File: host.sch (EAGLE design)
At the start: 25 parts, among them IC10 74LVC1T45W6-7, IC11 74LVC1T45W6-7, IC12 74LVC1T45W6-7, IC2 NCP187AMT120TAG, IC3 LD39200PU33R, IC8 74LVC1T45W6-7, Y1 DSC6001J

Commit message: Add the level changes (mostly, still need decoupling and connection to FPGA)
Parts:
- removed IC12: 74LVC1T45W6-7, samacsys:74LVC1T45W6-7
- added C13, C14, C15, C16, C17, C18: 100nF, rcl:C-EUC0201
- added IC1, IC4, IC5, IC6, IC9: 74LVC1T45GS,132, host:74LVC1T45GS,132
- added IC7: 74ALVC164245DGG:11, samacsys:74ALVC164245DGG_11
- IC10, IC11: value 74LVC1T45W6-7 -> 74LVC1T45GS,132; device samacsys:74LVC1T45W6-7 -> host:74LVC1T45GS,132; USE 74LVC1T45W6-7 -> (none)
- IC8: value 74LVC1T45W6-7 -> 74ALVC164245DGG:11; device samacsys:74LVC1T45W6-7 -> samacsys:74ALVC164245DGG_11; USE 74LVC1T45W6-7 -> 74ALVC164245DGG:11
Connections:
- new net !EXTSEL!: IC10.A
- new net !IRQ!: IC11.A
- new net !MPD!: IC9.A
- new net DIR_EXTSEL: IC10.DIR
- new net DIR_IRQ: IC11.DIR
- new net DIR_MPD: IC9.DIR
- net !A8_CCTL!: now also IC7.1B1
- net !A8_CLK!: now also IC7.1B2
- net !A8_D1XX!: now also IC7.1B0
- net !A8_EXTSEL!: now also IC10.B
- net !A8_HALT!: now also IC1.B; no longer IC8.B
- net !A8_IRQ!: now also IC11.B
- net !A8_MPD!: now also IC9.B
- net !A8_REF!: now also IC6.B; no longer IC10.B
- net !A8_RESET!: now also IC5.B; no longer IC11.B
- net !A8_S4!: now also IC7.1B5
- net !A8_S5!: now also IC7.1B4
- net !HALT!: now also IC1.A; no longer IC8.A
- net !REF!: now also IC6.A; no longer IC10.A
- net !RESET!: now also IC5.A; no longer IC11.A
- net +3V3: now also C14.1, C16.1, C18.1, IC1.VCC(A), IC4.VCC(A), IC5.VCC(A), IC6.VCC(A), IC9.VCC(A); no longer IC12.VCC(A), IC8.VCC(A)
- net +5V: now also C13.1, C15.1, C17.1, IC1.VCC(B), IC4.VCC(B), IC5.VCC(B), IC6.VCC(B), IC9.VCC(B); no longer IC12.VCC(B), IC8.VCC(B)
- net A8_A0: now also IC8.2B2
- net A8_A1: now also IC8.2B4
- net A8_A10: now also IC8.1B3
- net A8_A11: now also IC8.1B4
- net A8_A12: now also IC8.1B5
- net A8_A13: now also IC8.1B2
- net A8_A14: now also IC8.1B1
- net A8_A15: now also IC8.1B0
- net A8_A2: now also IC8.2B6
- net A8_A3: now also IC8.2B7
- net A8_A4: now also IC8.2B5
- net A8_A5: now also IC8.2B3
- net A8_A6: now also IC8.2B1
- net A8_A7: now also IC8.2B0
- net A8_A8: now also IC8.1B7
- net A8_A9: now also IC8.1B6
- net A8_D0: now also IC7.2B3
- net A8_D1: now also IC7.2B4
- net A8_D2: now also IC7.2B5
- net A8_D3: now also IC7.2B2
- net A8_D4: now also IC7.2B7
- net A8_D5: now also IC7.2B6
- net A8_D6: now also IC7.2B1
- net A8_D7: now also IC7.2B0
- net A8_R/!W!: now also IC4.B; no longer IC12.B
- net A8_RD4: now also IC7.1B6
- net A8_RD5: now also IC7.1B3
- net DIR_HALT: now also IC1.DIR; no longer IC8.DIR
- net DIR_REF: now also IC6.DIR; no longer IC10.DIR
- net DIR_RST: now also IC5.DIR; no longer IC11.DIR
- net DIR_RW: now also IC4.DIR; no longer IC12.DIR
- net GND: now also IC4.GND, IC5.GND, IC6.GND; no longer IC10.GND, IC11.GND, IC12.GND, IC8.GND
- net GND1: now also C13.2, C14.2, C15.2, C16.2, C17.2, C18.2, IC1.GND, IC10.GND, IC11.GND, IC9.GND
- net R/!W!: now also IC4.A; no longer IC12.A
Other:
- moved on the sheet: C10, C11, C12, C7, C8, C9, IC10, IC11

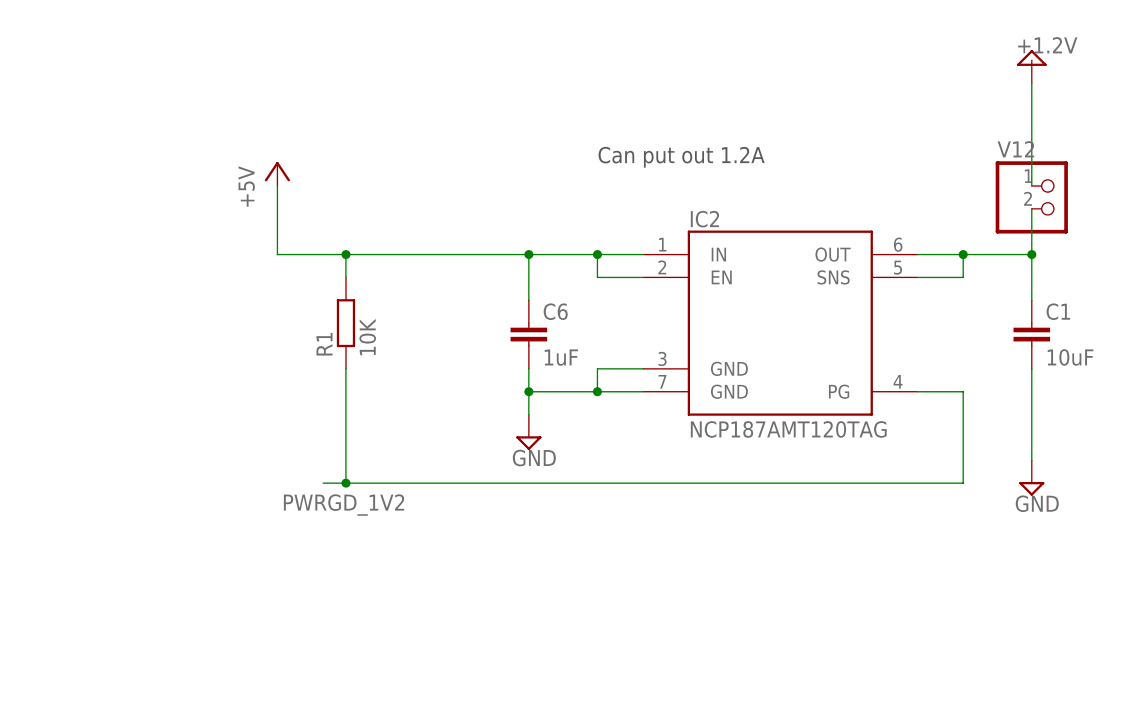
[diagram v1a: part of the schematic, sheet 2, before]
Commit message: Move to 6-layer board for supply cleanliness
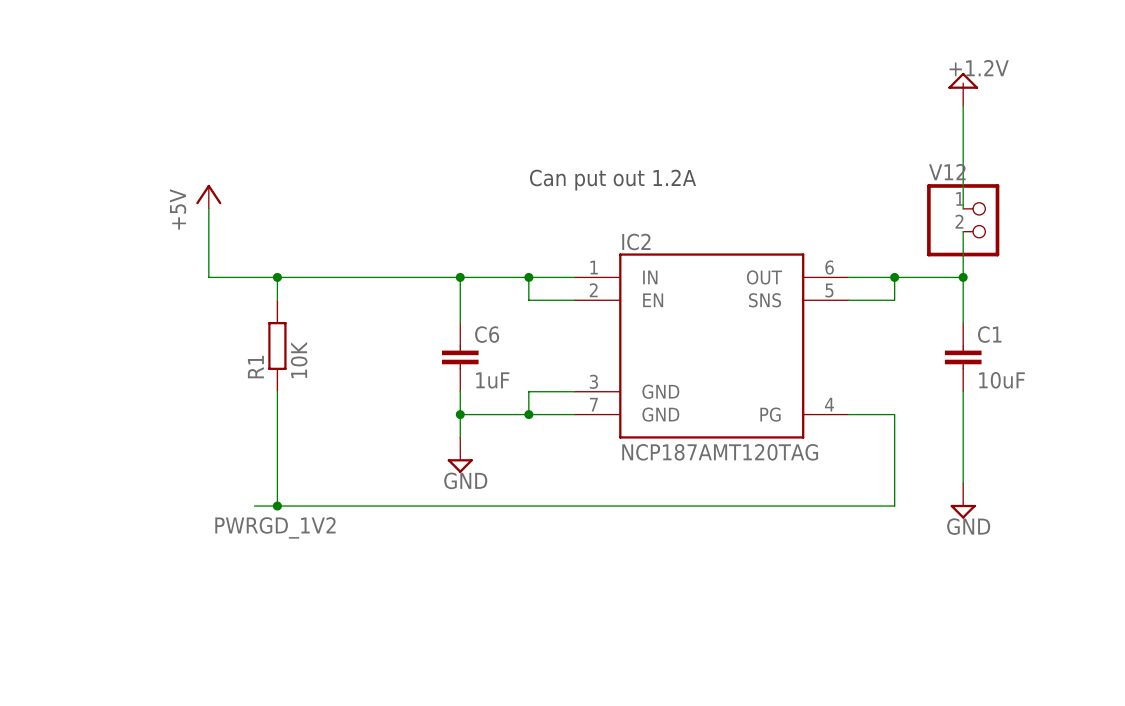
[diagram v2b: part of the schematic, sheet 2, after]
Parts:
- IC2: ARROW_PART_NUMBER (none) -> NCP187AMT120TAG
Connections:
- removed net GND1: C11.2, C12.2, C13.2, C14.2, C15.2, C16.2, C17.2, C18.2, IC1.GND, IC10.GND, IC11.GND, IC9.GND
- net +1.2V: now also U$1-CFG.VCC@125, U$1-CFG.VCC@128, U$1-CFG.VCC@13, U$1-CFG.VCC@130, U$1-CFG.VCC@22, U$1-CFG.VCC@49, U$1-CFG.VCC@57, U$1-CFG.VCC@85, U$1-CFG.VCC@96, U$1-CFG.VCCA_BR@73, U$1-LEFT.VCCA_TL@2, U$1-TOP.VCCA_TR@107
- net +5V: now also IC7.VCC(B)@18, IC7.VCC(B)@7, IC8.VCC(B)@18, IC8.VCC(B)@7
- net CLK25: now also U$1-TOP.GPIOR_157_PLLIN@75; no longer U$1-RIGHT.GPIOL_74_PLLIN0@132
- net GND: now also C11.2, C12.2, C13.2, C14.2, C15.2, C16.2, C17.2, C18.2, IC1.GND, IC10.GND, IC11.GND, IC9.GND
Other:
- moved on the sheet: C1, C6, IC2, R1, V12

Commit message: Hook up the level-translators to the FPGA
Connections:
- new net !CCTL!: IC7.1A1, U$1-RIGHT.GPIOR_85@111
- new net !D1XX!: IC7.1A0, U$1-RIGHT.GPIOR_86@112
- new net !S4!: IC7.1A5, U$1-RIGHT.GPIOR_79_EXTFB1_CDI30@118
- new net !S5!: IC7.1A4, U$1-RIGHT.GPIOR_80@117
- new net A0: IC8.2A2, U$1-LEFT.GPIOL_31_CLK7_CDI6@11
- new net A1: IC8.2A4, U$1-LEFT.GPIOL_24_CLK0@15
- new net A10: IC8.1A3, U$1-RIGHT.GPIOL_64@144
- new net A11: IC8.1A4, U$1-LEFT.GPIOL_53_CDI10@3
- new net A12: IC8.1A5, U$1-LEFT.GPIOL_54_CDI11@4
- new net A13: IC8.1A2, U$1-RIGHT.GPIOL_66_CDI12@142
- new net A14: IC8.1A1, U$1-RIGHT.GPIOL_65@141
- new net A15: IC8.1A0, U$1-RIGHT.GPIOL_67_CDI13@140
- new net A2: IC8.2A6, U$1-LEFT.GPIOL_21_CTRL1_CDI5@17
- new net A3: IC8.2A7, U$1-LEFT.GPIOL_20_CTRL0_CDI4@18
- new net A4: IC8.2A5, U$1-LEFT.GPIOL_22_CTRL2@16
- new net A5: IC8.2A3, U$1-LEFT.GPIOL_25_CLK1@14
- new net A6: IC8.2A1, U$1-LEFT.GPIOL_32_CTRL4_CDI7@10
- new net A7: IC8.2A0, U$1-LEFT.GPIOL_40_CDI8@8
- new net A8: IC8.1A7, U$1-LEFT.GPIOL_41_CDI9@7
- new net A9: IC8.1A6, U$1-LEFT.GPIOL_46@6
- new net CLK: IC7.1A2, U$1-RIGHT.GPIOR_84@113
- new net D0: IC7.2A3, U$1-RIGHT.GPIOL_74_PLLIN0@132
- new net D1: IC7.2A4, U$1-RIGHT.GPIOL_73_EXTFB1_CDI15@134
- new net D2: IC7.2A5, U$1-RIGHT.GPIOL_72_EXTFB0_CDI14@135
- new net D3: IC7.2A2, U$1-RIGHT.GPIOL_75_PLLIN1@131
- new net D4: IC7.2A7, U$1-RIGHT.GPIOL_70_CBSEL0@137
- new net D5: IC7.2A6, U$1-RIGHT.GPIOL_71_!STATUS!@136
- new net D6: IC7.2A1, U$1-RIGHT.GPIOR_76_PLLIN0@124
- new net D7: IC7.2A0, U$1-RIGHT.GPIOR_77_PLLIN1@123
- new net DIR_A: IC8.1DIR, IC8.2DIR, U$1-RIGHT.GPIOL_68@139
- new net DIR_D: IC7.2DIR, U$1-RIGHT.GPIOL_69_CBSEL1@138
- new net DIR_IN: IC7.1DIR, U$1-RIGHT.GPIOR_87_CDI29@110
- new net RD4: IC7.1A6, U$1-RIGHT.GPIOR_78_EXTFB0_CDI31@119
- new net RD5: IC7.1A3, U$1-RIGHT.GPIOR_83@114
- net !EXTSEL!: now also U$1-TOP.GPIOR_94_CDI27@106
- net !HALT!: now also U$1-TOP.GPIOR_116_CTRL15@99
- net !IRQ!: now also U$1-TOP.GPIOR_104_CDI25@103
- net !MPD!: now also U$1-TOP.GPIOR_122_CLK13_CDI21@97
- net !REF!: now also U$1-TOP.GPIOR_125_CLK10@92
- net !RESET!: now also U$1-TOP.GPIOR_112_CDI23@101
- net +3V3: now also U$1-LEFT.VCCIO1B@21, U$1-LEFT.VCCIO1C_1D@12, U$1-RIGHT.VCCIO1E@143, U$1-RIGHT.VCCIO3A@122, U$1-TOP.VCCIO3B_3C@95, U$1-TOP.VCCIO3D@91, U$1-TOP.VCCIO3E@88
- net DIR_EXTSEL: now also U$1-RIGHT.GPIOR_88_CDI28@109
- net DIR_HALT: now also U$1-TOP.GPIOR_113_CDI22@100
- net DIR_IRQ: now also U$1-TOP.GPIOR_95_CDI26@105
- net DIR_MPD: now also U$1-TOP.GPIOR_117_CTRL14@98
- net DIR_REF: now also U$1-TOP.GPIOR_123_CLK12_CDI20@93
- net DIR_RST: now also U$1-TOP.GPIOR_105_CDI24@102
- net DIR_RW: now also U$1-RIGHT.GPIOR_81_MREFCLK@116
- net GND: now also IC7.GND@10, IC7.GND@15, IC7.GND@21, IC7.GND@28, IC7.GND@34, IC7.GND@39, IC7.GND@4, IC7.GND@45, IC8.GND@10, IC8.GND@15, IC8.GND@21, IC8.GND@28, IC8.GND@34, IC8.GND@39, IC8.GND@4, IC8.GND@45
- net R/!W!: now also U$1-RIGHT.GPIOR_82@115
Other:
- note added: "OE on 8-bit LT's decoupling on 8-bit LTs SPI hookup in 4-bit mode pull resistors decoupling on FPGA USB-C connector TTAG / JTAG / SPI CDONE, CRESET, Leds"
- note removed: "input: CLK !CCTL! RD4 RD5 output: !MPD! !EXTSEL! !IRQ! inout: !RESET! R/!W! !HALT! !REF! A[0..15] D[0..7]"

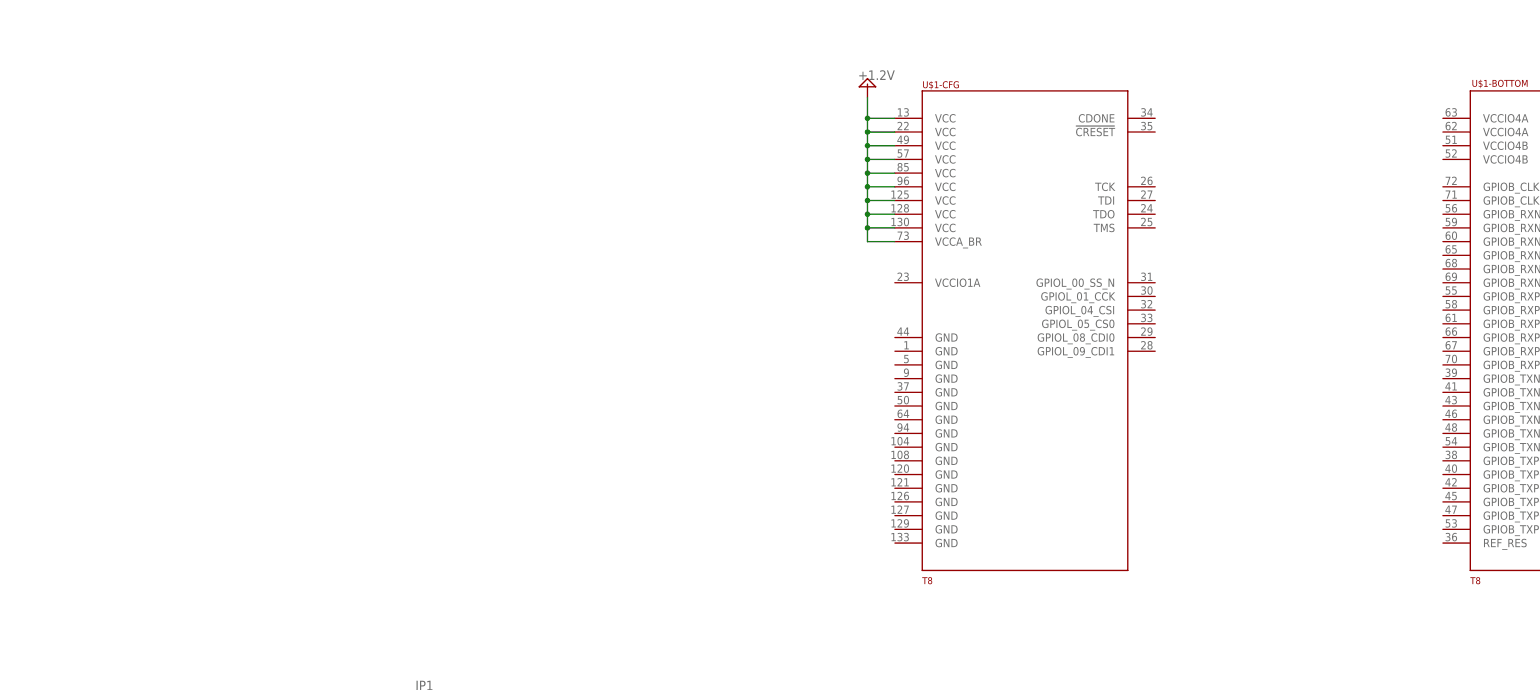
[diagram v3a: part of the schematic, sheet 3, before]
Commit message: Add FPGA decoupling caps
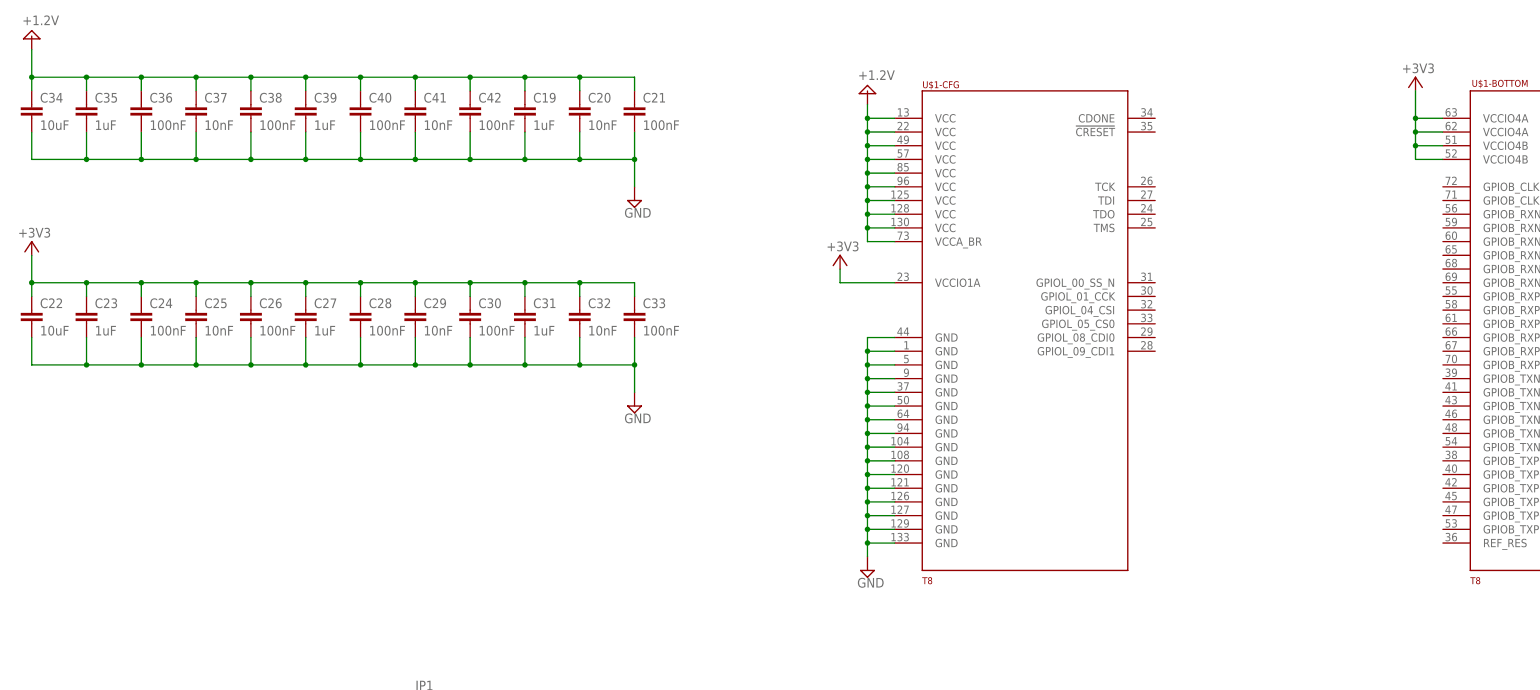
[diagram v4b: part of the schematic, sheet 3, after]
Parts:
- added C19, C23, C27, C31, C35, C39: 1uF, rcl:C-EUC0201
- added C20, C25, C29, C32, C37, C41: 10nF, rcl:C-EUC0201
- added C21, C24, C26, C28, C30, C33, C36, C38, C40, C42: 100nF, rcl:C-EUC0201
- added C22, C34: 10uF, rcl:C-EUC0402K
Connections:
- net +1.2V: now also C19.1, C20.1, C21.1, C34.1, C35.1, C36.1, C37.1, C38.1, C39.1, C40.1, C41.1, C42.1
- net +3V3: now also C22.1, C23.1, C24.1, C25.1, C26.1, C27.1, C28.1, C29.1, C30.1, C31.1, C32.1, C33.1, IC7.VCC(A)@31, IC7.VCC(A)@42, IC8.VCC(A)@31, IC8.VCC(A)@42, U$1-BOTTOM.VCCIO4A@62, U$1-BOTTOM.VCCIO4A@63, U$1-BOTTOM.VCCIO4B@51, U$1-BOTTOM.VCCIO4B@52, U$1-CFG.VCCIO1A@23
- net GND: now also C19.2, C20.2, C21.2, C22.2, C23.2, C24.2, C25.2, C26.2, C27.2, C28.2, C29.2, C30.2, C31.2, C32.2, C33.2, C34.2, C35.2, C36.2, C37.2, C38.2, C39.2, C40.2, C41.2, C42.2, IC7.!1OE, IC7.!2OE, IC8.!1OE, IC8.!2OE, U$1-CFG.GND@1, U$1-CFG.GND@104, U$1-CFG.GND@108, U$1-CFG.GND@120, U$1-CFG.GND@121, U$1-CFG.GND@126, U$1-CFG.GND@127, U$1-CFG.GND@129, U$1-CFG.GND@133, U$1-CFG.GND@37, U$1-CFG.GND@44, U$1-CFG.GND@5, U$1-CFG.GND@50, U$1-CFG.GND@64, U$1-CFG.GND@9, U$1-CFG.GND@94
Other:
- note added: "Expose SPI pins for external programming Use the Efinix transistor on CDONE"
- note added: "decoupling on 8-bit LTs SPI hookup in 4-bit mode pull resistors USB-C connector TTAG / JTAG / SPI CDONE, CRESET, Leds"
- note removed: "Clock goes to PLL_IN0, either one Need level changers Expose SPI pins for external programming Use the Efinix transistor on CDONE"
- note removed: "OE on 8-bit LT's decoupling on 8-bit LTs SPI hookup in 4-bit mode pull resistors decoupling on FPGA USB-C connector TTAG / JTAG / SPI CDONE, CRESET, Leds"

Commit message: Add level-translation decoupling caps
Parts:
- added C43, C44, C45, C46, C47, C48, C49, C50: 100nF, rcl:C-EUC0201
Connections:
- net +3V3: now also C43.1, C44.1, C45.1, C46.1
- net +5V: now also C47.1, C48.1, C49.1, C50.1
- net GND: now also C43.2, C44.2, C45.2, C46.2, C47.2, C48.2, C49.2, C50.2
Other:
- note added: "SPI flash SPI hookup in 4-bit mode DIR_*, SPI, JTAG pull resistors USB-C connector TTAG / JTAG / SPI CDONE, CRESET, Leds Use the Efinix transistor on CDONE"
- note removed: "Expose SPI pins for external programming Use the Efinix transistor on CDONE"
- note removed: "decoupling on 8-bit LTs SPI hookup in 4-bit mode pull resistors USB-C connector TTAG / JTAG / SPI CDONE, CRESET, Leds"

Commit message: Working through the design-guide
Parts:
- added C51, C53: 100nF, rcl:C-EUC0201
- added C52: 10uF, rcl:C-EUC0402K
- added CBSEL0, CBSEL1, CBUS0, CBUS1, CBUS2: (no value), pinhead:PINHD-1X3
- added FLASH: W25Q32JVSSIQ, SparkFun:SPI_FLASH-X25XXSMD
- added R10, R11, R12, R13, R14, R15, R16, R17, R18, R19, R2, R20, R21, R22, R23, R24, R25, R26, R27, R28, R3, R4, R5, R6, R7, R8, R9: 10K, rcl:R-EU_R0201
- added RESET: (no value), SparkFun:TAC_SWITCHPTH
- added SPV: MIC803-30D2VC3-TR, x-pi:MIC803-30D2VM3-TR
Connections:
- new net !CRESET!: C52.1, JP1.CRESET@5, R9.2, RESET.3, RESET.4, SPV.!RESET!@2, U$1-CFG.!CRESET!@35
- new net !STATUS!: JP1.!STATUS!@6
- new net !TEST!: R5.2, U$1-TOP.GPIOR_158_!TEST!@74
- new net CBSEL0: R23.2, U$1-RIGHT.GPIOL_70_CBSEL0@137
- new net CBSEL1: R24.2, U$1-RIGHT.GPIOL_69_CBSEL1@138
- new net CBUS0: R6.2, U$1-TOP.GPIOR_151_CBUS0@78
- new net CBUS1: R7.2, U$1-TOP.GPIOR_150_CBUS1@79
- new net CBUS2: R8.2, U$1-TOP.GPIOR_149_CBUS2@80
- new net CDONE: JP1.CDONE@3, R3.2, U$1-CFG.CDONE@34
- new net N$1: CBSEL0.2, R23.1
- new net N$10: CBUS0.2, R6.1
- new net N$11: CBUS1.2, R7.1
- new net N$12: CBUS2.2, R8.1
- new net N$3: CBSEL1.2, R24.1
- new net SPI_CLK: FLASH.SCK, JP1.SCLK@13, U$1-CFG.GPIOL_01_CCK@30
- new net SPI_CSI: R2.2, U$1-CFG.GPIOL_04_CSI@32
- new net SPI_D0: FLASH.MOSI, JP1.MOSI@11, U$1-CFG.GPIOL_08_CDI0@29
- new net SPI_D1: FLASH.MISO, JP1.MISO@9, U$1-CFG.GPIOL_09_CDI1@28
- new net SPI_D2: FLASH.WP, U$1-LEFT.GPIOL_12_CDI2@20
- new net SPI_D3: FLASH.HOLD, JP1.HOLD@1, U$1-LEFT.GPIOL_13_CDI3@19
- new net SPI_SS: FLASH.CS, JP1.!CS!@7, R4.2, U$1-CFG.GPIOL_00_SS_N@31
- new net TCK: JP1.TCK@8, R28.2, U$1-CFG.TCK@26
- new net TDI: JP1.TDI@14, R26.2, U$1-CFG.TDI@27
- new net TDO: JP1.TDO@12, R27.2, U$1-CFG.TDO@24
- new net TMS: JP1.TMS@10, R25.2, U$1-CFG.TMS@25
- net !CCTL!: now also U$1-RIGHT.GPIOR_88_CDI28@109; no longer U$1-RIGHT.GPIOR_85@111
- net !D1XX!: now also U$1-TOP.GPIOR_104_CDI25@103; no longer U$1-RIGHT.GPIOR_86@112
- net !EXTSEL!: now also R22.1, U$1-TOP.GPIOR_113_CDI22@100; no longer U$1-TOP.GPIOR_94_CDI27@106
- net !HALT!: now also U$1-TOP.GPIOR_123_CLK12_CDI20@93; no longer U$1-TOP.GPIOR_116_CTRL15@99
- net !IRQ!: now also R21.1, U$1-TOP.GPIOR_95_CDI26@105; no longer U$1-TOP.GPIOR_104_CDI25@103
- net !MPD!: now also R20.1, U$1-TOP.GPIOR_128_CTRL11@90; no longer U$1-TOP.GPIOR_122_CLK13_CDI21@97
- net !REF!: now also U$1-TOP.GPIOR_132_CDI19@87; no longer U$1-TOP.GPIOR_125_CLK10@92
- net !RESET!: now also U$1-TOP.GPIOR_117_CTRL14@98; no longer U$1-TOP.GPIOR_112_CDI23@101
- net !S4!: now also U$1-RIGHT.GPIOR_82@115; no longer U$1-RIGHT.GPIOR_79_EXTFB1_CDI30@118
- net !S5!: now also U$1-RIGHT.GPIOR_83@114; no longer U$1-RIGHT.GPIOR_80@117
- net +3V3: now also C51.1, C53.1, CBSEL0.1, CBSEL1.1, CBUS0.1, CBUS1.1, CBUS2.1, FLASH.VCC, R17.2, R18.2, R19.2, R2.1, R20.2, R21.2, R22.2, R25.1, R26.1, R27.1, R28.1, R3.1, R4.1, R5.1, R9.1, SPV.VCC@3
- net CLK: now also U$1-RIGHT.GPIOR_87_CDI29@110; no longer U$1-RIGHT.GPIOR_84@113
- net D0: now also U$1-RIGHT.GPIOR_77_PLLIN1@123; no longer U$1-RIGHT.GPIOL_74_PLLIN0@132
- net D1: now also U$1-RIGHT.GPIOR_76_PLLIN0@124; no longer U$1-RIGHT.GPIOL_73_EXTFB1_CDI15@134
- net D2: now also U$1-RIGHT.GPIOL_75_PLLIN1@131; no longer U$1-RIGHT.GPIOL_72_EXTFB0_CDI14@135
- net D3: now also U$1-RIGHT.GPIOR_78_EXTFB0_CDI31@119; no longer U$1-RIGHT.GPIOL_75_PLLIN1@131
- net D4: now also U$1-RIGHT.GPIOL_73_EXTFB1_CDI15@134; no longer U$1-RIGHT.GPIOL_70_CBSEL0@137
- net D5: now also U$1-RIGHT.GPIOL_74_PLLIN0@132; no longer U$1-RIGHT.GPIOL_71_!STATUS!@136
- net D6: now also U$1-RIGHT.GPIOR_79_EXTFB1_CDI30@118; no longer U$1-RIGHT.GPIOR_76_PLLIN0@124
- net D7: now also U$1-RIGHT.GPIOR_80@117; no longer U$1-RIGHT.GPIOR_77_PLLIN1@123
- net DIR_A: now also R10.2
- net DIR_D: now also R11.2, U$1-RIGHT.GPIOL_72_EXTFB0_CDI14@135; no longer U$1-RIGHT.GPIOL_69_CBSEL1@138
- net DIR_EXTSEL: now also R17.1, U$1-TOP.GPIOR_94_CDI27@106; no longer U$1-RIGHT.GPIOR_88_CDI28@109
- net DIR_HALT: now also R13.2, U$1-TOP.GPIOR_122_CLK13_CDI21@97; no longer U$1-TOP.GPIOR_113_CDI22@100
- net DIR_IN: now also R12.2, U$1-TOP.GPIOR_105_CDI24@102; no longer U$1-RIGHT.GPIOR_87_CDI29@110
- net DIR_IRQ: now also R18.1, U$1-TOP.GPIOR_116_CTRL15@99; no longer U$1-TOP.GPIOR_95_CDI26@105
- net DIR_MPD: now also R19.1, U$1-TOP.GPIOR_125_CLK10@92; no longer U$1-TOP.GPIOR_117_CTRL14@98
- net DIR_REF: now also R15.2, U$1-TOP.GPIOR_129_CTRL10@89; no longer U$1-TOP.GPIOR_123_CLK12_CDI20@93
- net DIR_RST: now also R14.2, U$1-TOP.GPIOR_112_CDI23@101; no longer U$1-TOP.GPIOR_105_CDI24@102
- net DIR_RW: now also R16.2, U$1-RIGHT.GPIOR_84@113; no longer U$1-RIGHT.GPIOR_81_MREFCLK@116
- net GND: now also C51.2, C52.2, C53.2, CBSEL0.3, CBSEL1.3, CBUS0.3, CBUS1.3, CBUS2.3, FLASH.GND, JP1.GND@2, JP1.GND@4, R10.1, R11.1, R12.1, R13.1, R14.1, R15.1, R16.1, RESET.1, RESET.2, SPV.GND@1
- net R/!W!: now also U$1-RIGHT.GPIOR_85@111; no longer U$1-RIGHT.GPIOR_82@115
- net RD4: now also U$1-RIGHT.GPIOR_81_MREFCLK@116; no longer U$1-RIGHT.GPIOR_78_EXTFB0_CDI31@119
- net RD5: now also U$1-RIGHT.GPIOR_86@112; no longer U$1-RIGHT.GPIOR_83@114
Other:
- note added: "DIR_*, SPI, JTAG pull resistors USB-C connector TTAG / JTAG / SPI CDONE, CRESET, Leds, STATUS Use the Efinix transistor on CDONE"
- note removed: "SPI flash SPI hookup in 4-bit mode DIR_*, SPI, JTAG pull resistors USB-C connector TTAG / JTAG / SPI CDONE, CRESET, Leds Use the Efinix transistor on CDONE"
